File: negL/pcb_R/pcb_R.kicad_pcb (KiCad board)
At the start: 2 copper layers, 168.4 x 117.5 mm, 149 parts, among them IC1 SN74LVC4245APWR, J1 MJ-4PP-9, J2 FH-1x4SG/RH, J3 XA-3-2-7P, Q1 AO3400A, Q2 AO3400A, Q3 AO3401A, SW1 TVBP06-B043CB-B, SW2 EVQWGD001_EC12, SW3 SS-12D00G3, SW4 SS-12D00G3, U1 nice_nano, U2 74HC595D,112, U3 TPS61023DRLR, U4 TPS61021ADSGR, U6 LM66100DCKR

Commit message: v0.1 rc
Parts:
- removed the C2 at (74.4, 103.7)
- removed IC1: SN74LVC4245APWR, Package_SO:TSSOP-24_4.4x7.8mm_P0.65mm
- added C4: CL10A226MP8NUNE, Capacitor_SMD:C_0603_1608Metric, B.Cu at (75.0, 93.7)
- added C6: CL10A226MP8NUNE, Capacitor_SMD:C_0603_1608Metric, B.Cu at (74.6, 101.9)
- added C7: CL10A226MP8NUNE, Capacitor_SMD:C_0603_1608Metric, B.Cu at (74.7, 103.5)
- added JP17: ~, Jumper:SolderJumper-2_P1.3mm_Open_Pad1.0x1.5mm, B.Cu at (95.2, 89.3)
- added JP18: ~, Jumper:SolderJumper-2_P1.3mm_Open_Pad1.0x1.5mm, B.Cu at (100.0, 89.3)
- added U6: SN74LVC1T45DBVT, Package_TO_SOT_SMD:SOT-23-6, B.Cu at (76.1, 125.3)
- C3: renamed from C4; value GRM32ER61A107ME20L -> CL10A226MP8NUNE; footprint Capacitor_SMD:C_1210_3225Metric -> Capacitor_SMD:C_0603_1608Metric
- C5: renamed from C1; value C1608X5R1A225K080AC -> GRM21BR61A226ME44L; footprint Capacitor_SMD:C_0603_1608Metric -> Capacitor_SMD:C_0805_2012Metric
- Q1, Q2: value AO3400A -> DMN1008UFDF-7; footprint Package_TO_SOT_SMD:SOT-23 -> Package_DFN_QFN:Diodes_UDFN2020-6_Type-F
- Q3: value AO3401A -> DMP1022UFDF-7; footprint Package_TO_SOT_SMD:SOT-23 -> Package_DFN_QFN:Diodes_UDFN2020-6_Type-F
- R4: value RC0603FR-07732KL -> RC0603FR-07619KL
- U2: value 74HC595D,112 -> 74HC595D,118
- moved MT10 13.1 mm to (165.5, 111.9)
- moved MT8 13.1 mm to (127.4, 111.9)
- moved JP11 12.4 mm to (83.3, 118.5)
- moved MT11 8.33 mm to (203.6, 57.1)
- moved MT9 8.33 mm to (165.5, 52.4)
- moved JP13 8.01 mm to (73.8, 119.1), turned to 0 degrees
- moved JP12 7.71 mm to (79.1, 119.1), turned to 0 degrees
- moved R5 6.03 mm to (80.4, 97.6), turned to 0 degrees
- moved L2 4.92 mm to (73.8, 81.0)
- moved R7 4.91 mm to (100.0, 92.9)
- moved R6 4.83 mm to (96.4, 92.9)
- moved Q2 3.58 mm to (74.0, 62.9), turned to 180 degrees
- moved R3 3.57 mm to (102.1, 96.4)
- moved R4 3.55 mm to (76.0, 98.5), turned to 0 degrees
- moved Q1 3.32 mm to (74.1, 60.0), turned to 0 degrees
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- renumbered C3 to C1, C5 to C2, MT9 to MT10, MT10 to MT11, MT11 to MT12, MT12 to MT5, MT5 to MT6, MT6 to MT7, MT7 to MT8, MT8 to MT9, R6 to R1, R7 to R2, R2 to R6, R1 to R7, U6 to U5
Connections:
- JP12 pad 1: VCC -> Net-(JP12-A)
- JP12 pad 2: Net-(IC1-~{OE}) -> GND
- JP13 pad 1: Net-(IC1-~{OE}) -> VCC
- JP13 pad 2: GND -> Net-(JP12-A)
- Q1 pad 1: Net-(Q1-G) -> Net-(Q1-D-Pad1)
- Q1 pad 2: Net-(BT1--) -> Net-(Q1-D-Pad1)
- Q1 pad 3: Net-(Q1-D) -> Net-(Q1-G)
- Q2 pad 1: Net-(Q1-G) -> Net-(Q1-D-Pad1)
- Q2 pad 2: Net-(JP1-B) -> Net-(Q1-D-Pad1)
- Q2 pad 3: Net-(Q1-D) -> Net-(Q1-G)
- Q3 pad 1: Net-(Q3-G) -> LED_VCC
- Q3 pad 2: Net-(JP14-B) -> LED_VCC
- Q3 pad 3: LED_VCC -> Net-(Q3-G)
- R6 pad 2: DISP_SDA -> Net-(JP17-B)
- R7 pad 2: DISP_SCL -> Net-(JP18-B)
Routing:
- net GND: track 841.1 -> 867.1 mm, vias 107 -> 115
- net Net-(JP12-A): track 0.00 -> 12.8 mm
- net Net-(Q1-D-Pad1): track 0.00 -> 9.58 mm
- net Net-(BT1--): track 96.0 -> 105.2 mm, vias 1 -> 2
- net LED_VCC: track 684.0 -> 691.7 mm, vias 7 -> 9
- net Net-(IC1-~{OE}): track 7.08 -> 0.00 mm
- net Net-(Q1-G): track 9.60 -> 14.1 mm, vias 0 -> 2
- net Net-(Q1-D): track 4.01 -> 0.00 mm
- net Net-(JP17-B): track 0.00 -> 3.99 mm
- net Net-(JP14-B): track 4.27 -> 8.07 mm
- net Net-(JP18-B): track 0.00 -> 3.64 mm
- net LED_CUTOFF: track 60.4 -> 56.8 mm
- net Net-(LED3-DOUT): track 94.0 -> 97.4 mm
- net Net-(U3-FB): track 7.92 -> 5.27 mm, vias 2 -> 0
- net Net-(L2-Pad2): track 6.93 -> 9.20 mm
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- added copper zone on B.Cu, net Net-(BT1--)
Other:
- outline, holes or cut-outs redrawn
- board text added: "- +"

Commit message: v0.1
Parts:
- C5: value GRM21BR61A226ME44L -> GRM21BR61C226ME44L

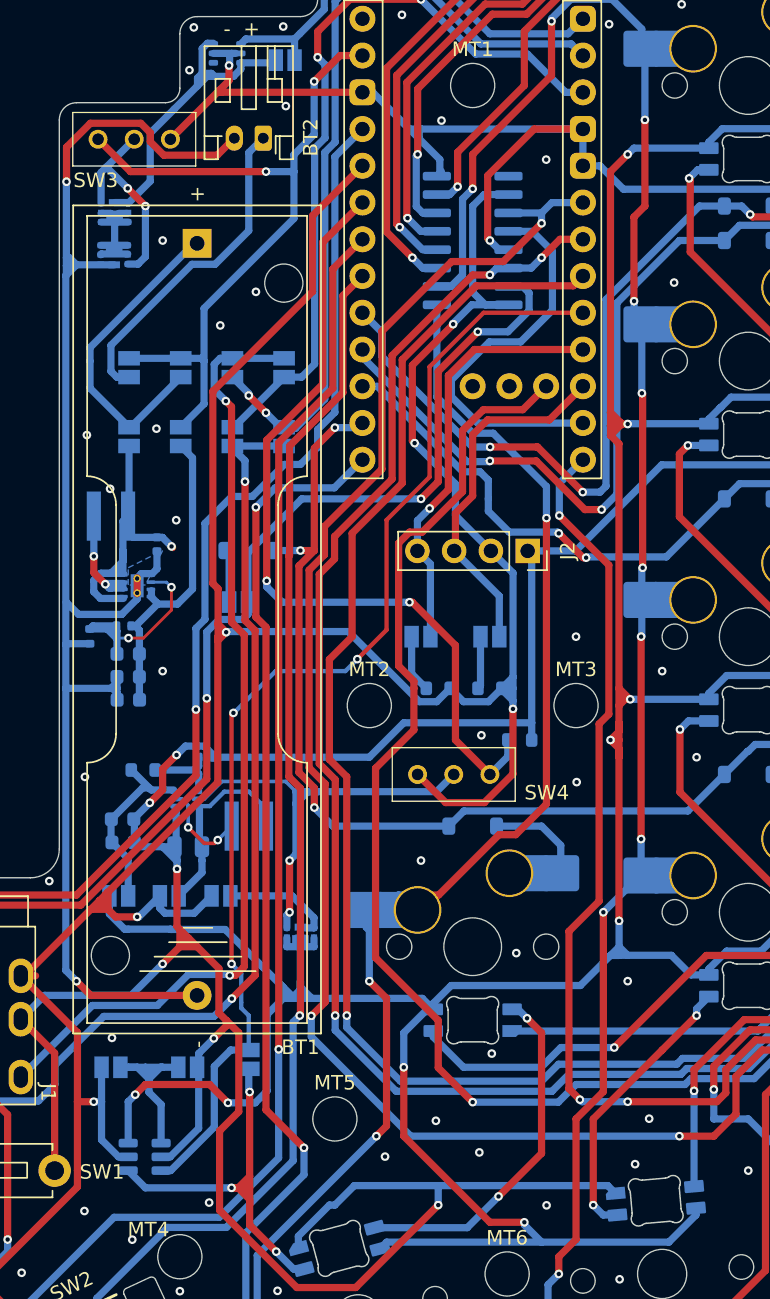
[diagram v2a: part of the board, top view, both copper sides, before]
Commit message: fix(pcb/right): Fixed critical bug that power switch not working
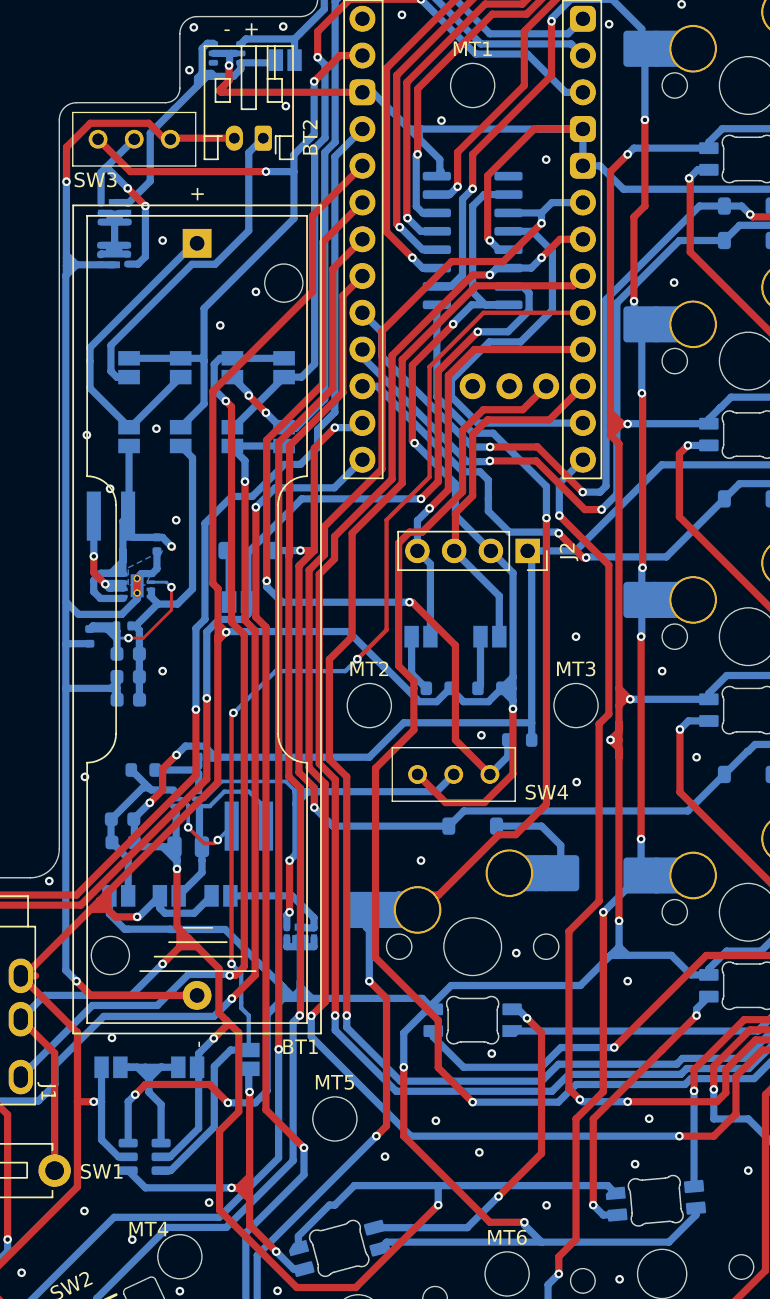
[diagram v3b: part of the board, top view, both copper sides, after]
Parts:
- C5: value GRM21BR61C226ME44L -> GRM21BR61A226ME44L
- L1: value XFL4020-102MEB -> XAL4020-102MEC
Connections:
- SW3 pad 3: GND -> Net-(BT1--)
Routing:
- net GND: track 867.1 -> 862.4 mm
- net Net-(BT1--): track 105.2 -> 103.9 mm
